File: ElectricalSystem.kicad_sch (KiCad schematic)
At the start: 2 parts, among them SW3 Supp_Enable

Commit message: update pedals
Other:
- sheet Pedal_Board ports: added Accel_Pot, Brake_Fluid, Brake_Pot; removed +3.3V_Accel, +3.3V_Brake, GND_Accel, GND_Brake, Sens_Accel, Sens_Brake
- note added: "- Controls Daughter Board - Steering board - Fans - Battery boards (internal HV?) - Telemetry sensors/leader - Array (MPPTs, Blackbody sensors) - VCU + MotorCAN? - Explain purpose of each CAN - Diagram CAN loop topology"
- note removed: "- Controls Daughter Board - Update pedals - Steering board - Fans - Battery boards (internal HV?) - Telemetry sensors/leader - Array (MPPTs, Blackbody sensors) - VCU + MotorCAN? - Explain purpose of each CAN - Diagram CAN loop topology"

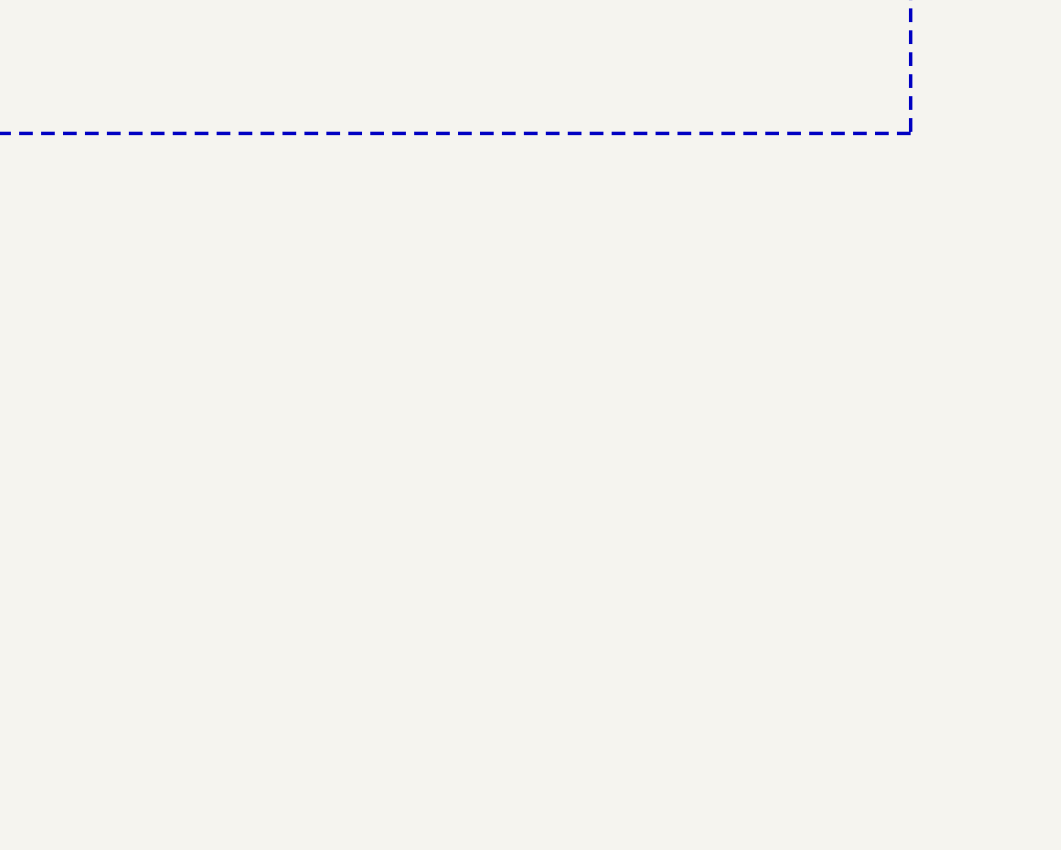
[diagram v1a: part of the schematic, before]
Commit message: start adding CAN topology notes
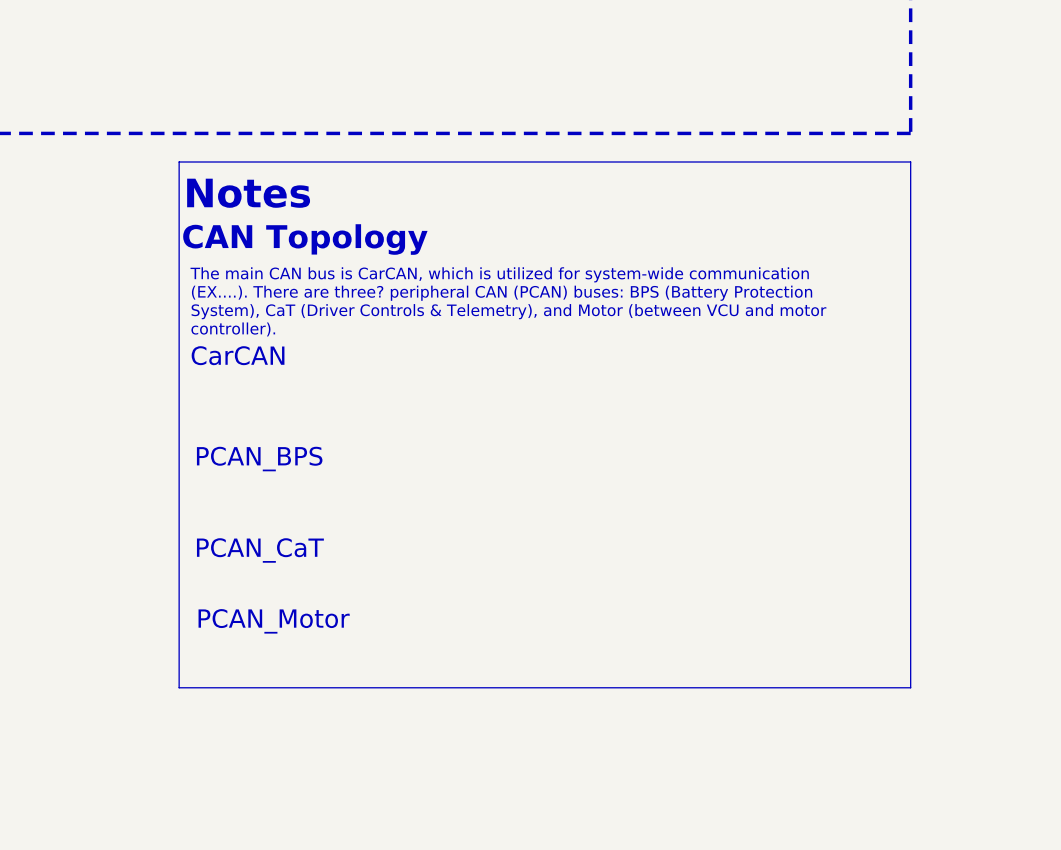
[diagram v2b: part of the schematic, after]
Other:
- note added: "CAN Topology"
- note added: "CarCAN"
- note added: "Notes"
- note added: "PCAN_BPS"
- note added: "PCAN_CaT"
- note added: "PCAN_Motor"
- note added: "The main CAN bus is CarCAN, which is utilized for system-wide communication (EX....). There are three? peripheral CAN (PCAN) buses: BPS (Battery Protection System), CaT (Driver Controls & Telemetry), and Motor (between VCU and motor controller)."
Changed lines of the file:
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@@
+	)
+	(rectangle
+		(start 462.28 137.16)
+		(end 543.56 195.58)
+		(stroke
+			(width 0)
+			(type default)
+		)
+		(fill
+			(type none)
+		)
 	)
 	(rectangle
@@
 		)
 	)
+	(text "The main CAN bus is CarCAN, which is utilized for system-wide communication\n(EX....). There are three? peripheral CAN (PCAN) buses: BPS (Battery Protection\nSystem), CaT (Driver Controls & Telemetry), and Motor (between VCU and motor\ncontroller)."
+		(exclude_from_sim no)
+		(at 463.55 152.908 0)
+		(effects
+			(font
+				(size 1.27 1.27)
+			)
+			(justify left)
+		)
+	)
 	(text "BPS"
 		(exclude_from_sim no)
@@
 		)
 	)
+	(text "CAN Topology"
+		(exclude_from_sim no)
+		(at 476.25 145.796 0)
+		(effects
+			(font
+				(size 2.54 2.54)
+				(bold yes)
+			)
+		)
+	)
 	(text "PDU and PowerBoard may be combined - TBD"
 		(exclude_from_sim no)
@@
 		)
 	)
+	(text "PCAN_Motor"
+		(exclude_from_sim no)
+		(at 472.694 188.214 0)
+		(effects
+			(font
+				(size 2.032 2.032)
+				(thickness 0.254)
+			)
+		)
+	)
 	(text "Cooling"
 		(exclude_from_sim no)
@@
 		)
 	)
+	(text "Notes"
+		(exclude_from_sim no)
+		(at 469.9 140.97 0)
+		(effects
+			(font
+				(size 3.175 3.175)
+				(bold yes)
+			)
+		)
+	)
 	(text "- Controls Daughter Board\n- Steering board\n- Fans\n- Battery boards (internal HV?)\n- Telemetry sensors/leader\n- Array (MPPTs, Blackbody sensors)\n- VCU + MotorCAN?\n- Explain purpose of each CAN\n- Diagram CAN loop topology"
 		(exclude_from_sim no)
@@
 		)
 	)
+	(text "PCAN_BPS"
+		(exclude_from_sim no)
+		(at 471.17 170.18 0)
+		(effects
+			(font
+				(size 2.032 2.032)
+				(thickness 0.254)
+			)
+		)
+	)
 	(text "add contactors, internal battery architecture, bus bar connections"
 		(exclude_from_sim no)
@@
 		)
 	)
+	(text "PCAN_CaT"
+		(exclude_from_sim no)
+		(at 471.17 180.34 0)
+		(effects
+			(font
+				(size 2.032 2.032)
+				(thickness 0.254)
+			)
+		)
+	)
 	(text "TODO:\n"
 		(exclude_from_sim no)
@@
 			)
 		)
+	)
+	(text "CarCAN"
+		(exclude_from_sim no)
+		(at 468.884 159.004 0)
+		(effects
+			(font
+				(size 2.032 2.032)
+				(thickness 0.254)
+			)
+		)

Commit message: add LV pwr dist
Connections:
- net SupplementalBattery/+12V_Supp: no longer SW3.1 (A)
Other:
- added sheet PeripheralSOM10 (PeripheralSOM.kicad_sch)
- added sheet PeripheralSOM11 (PeripheralSOM.kicad_sch)
- sheet Display_Screen ports: added LV_PWR; removed none
- sheet PowerDistributionBoard ports: added none; removed +5V_CarCAN, +CarCAN, -CarCAN, GND_CarCAN
- sheet SuppMonitoringBoard ports: added none; removed +5V_CarCAN, +CarCAN, -CarCAN, GND_CarCAN
- note added: "LV Power Distribution"
- note added: "Supp Enable switch on dashboard"
- moved on the sheet: SW3

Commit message: more stuff idk
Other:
- note added: "Array"
- note added: "HV Power Distribution"
- note added: "Main Battery Pack"
- note added: "Telemetry"
- note added: "add MPPTs, interface, blackbody A/C (temp/irradiance sensors)"
- note added: "add dynamics, environment, TPMS transceiver, broker?"
- note added: "replace with VCU and new architecture"
- note removed: "Battery"
- moved on the sheet: SW3

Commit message: heheheheh
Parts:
- added M1: Motor_BLDC, symbol Motor:Motor_DC
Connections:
- new net MotorController/PhaseA: M1.A (PhaseA)
- new net MotorController/PhaseB: M1.B (PhaseB)
- new net MotorController/PhaseC: M1.C (PhaseC)
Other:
- sheet MotorController ports: added DC+, DC-, PhaseA, PhaseB, PhaseC; removed none

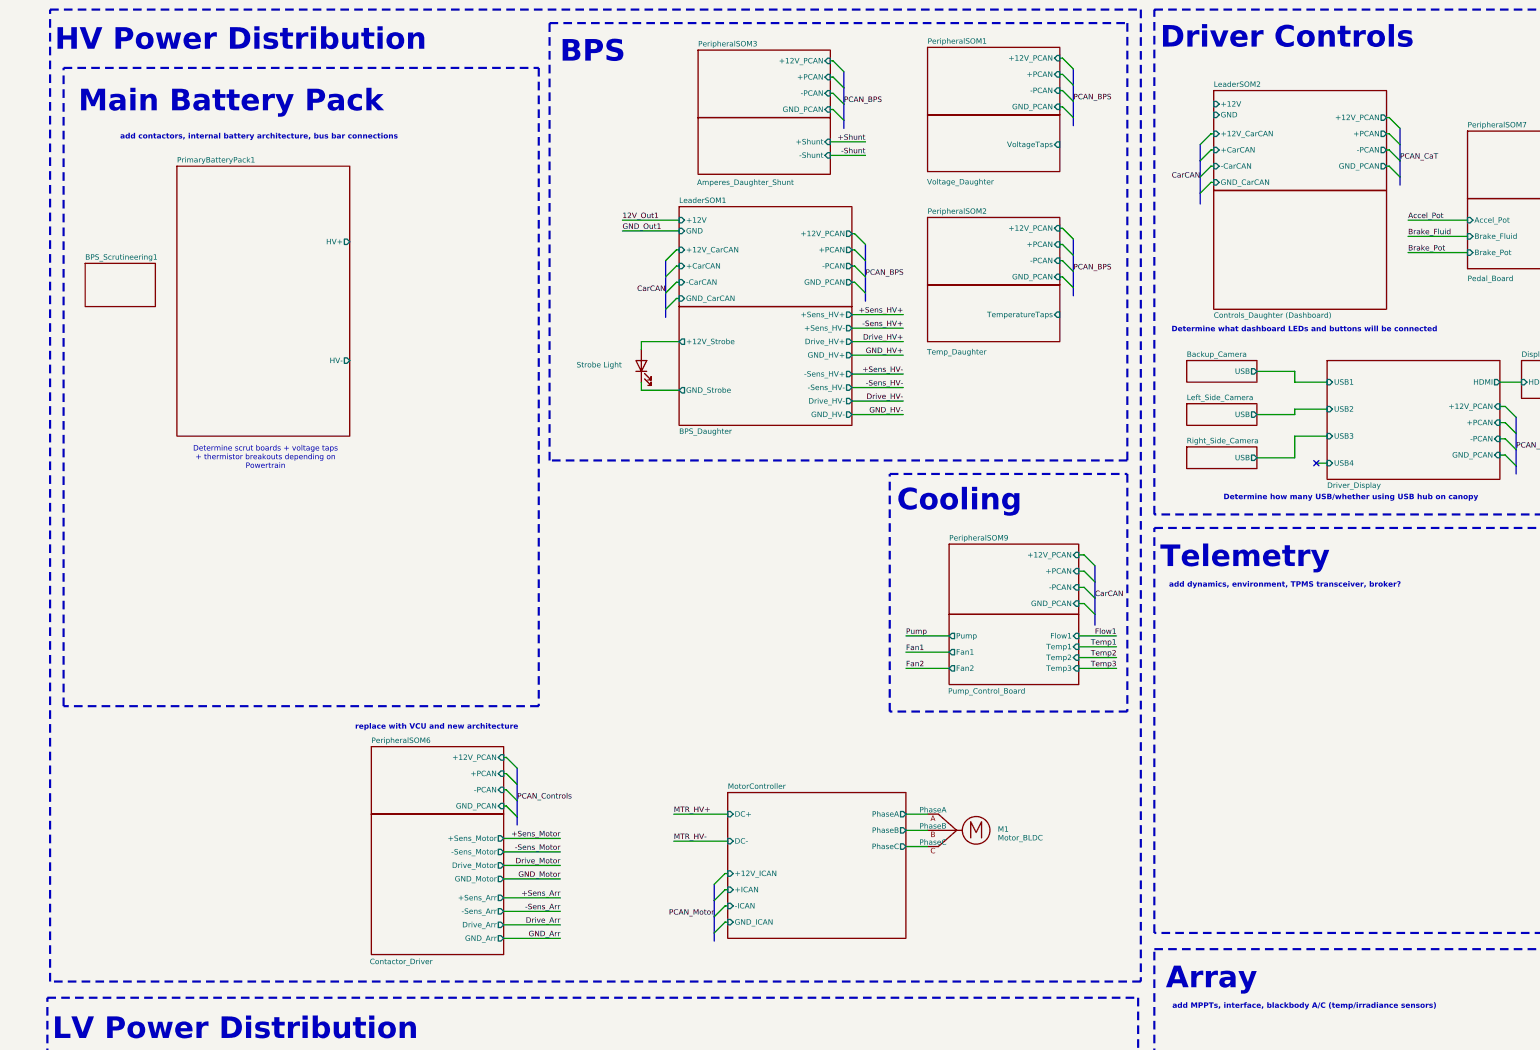
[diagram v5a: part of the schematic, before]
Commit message: moco intfc
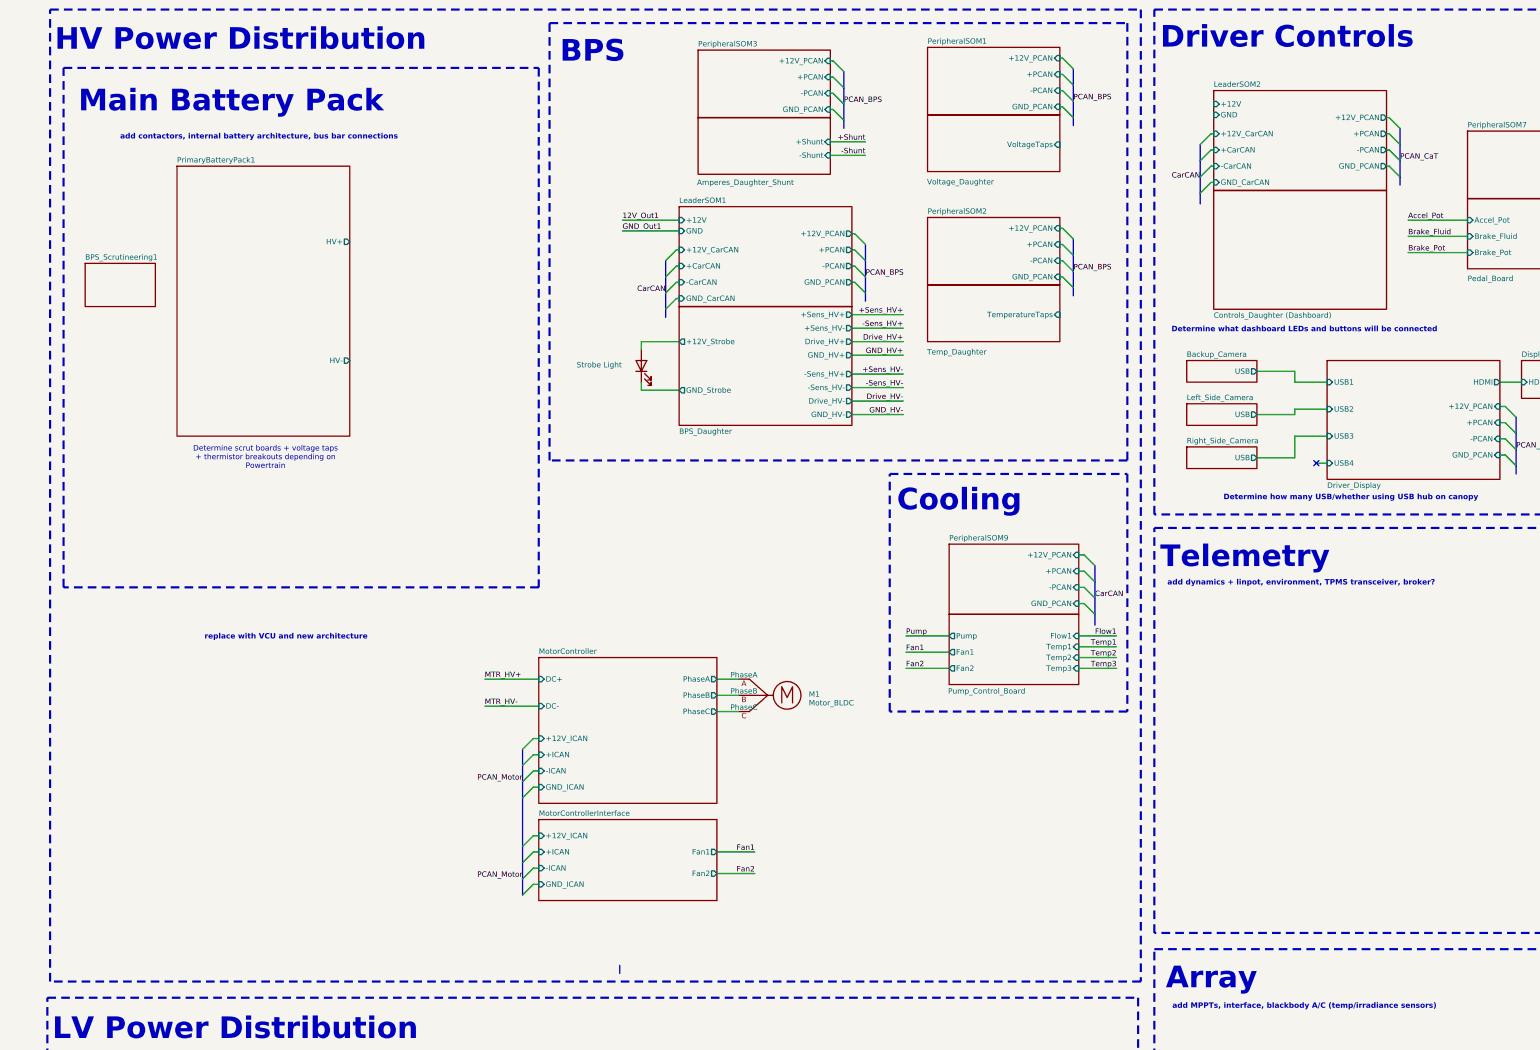
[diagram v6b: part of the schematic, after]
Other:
- removed sheet Contactor_Driver
- removed sheet PeripheralSOM6
- added sheet MotorControllerInterface (MotorControllerInterface.kicad_sch)
- note added: "add dynamics + linpot, environment, TPMS transceiver, broker?"
- note removed: "add dynamics, environment, TPMS transceiver, broker?"
- moved on the sheet: M1

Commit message: add mppts
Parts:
- added SC1, SC2, SC3: WHICH SUB ARRAY IS THIS, symbol Device:Solar_Cells
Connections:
- new net MPPT_A/PV+: SC1.1 (+)
- new net MPPT_A/PV-: SC1.2 (-)
- new net MPPT_B/PV+: SC2.1 (+)
- new net MPPT_B/PV-: SC2.2 (-)
- new net MPPT_C/PV+: SC3.1 (+)
- new net MPPT_C/PV-: SC3.2 (-)
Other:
- added sheet LeaderSOM3 (LeaderSOM.kicad_sch)
- added sheet MPPT_A (MPPT.kicad_sch)
- added sheet MPPT_B (MPPT.kicad_sch)
- added sheet MPPT_C (MPPT.kicad_sch)
- added sheet Steering_Board (Steering_Board.kicad_sch)
- added sheet VehicleControlUnit (VehicleControlUnit.kicad_sch)
- note added: "not sure if any of this needs isolation - check again!"

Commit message: wiring stuff
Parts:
- SC1: value WHICH SUB ARRAY IS THIS -> Rear_SubArray
- SC2: value WHICH SUB ARRAY IS THIS -> FrontRight_SubArray
- SC3: value WHICH SUB ARRAY IS THIS -> FrontLeft_SubArray
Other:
- sheet Display_Screen ports: added +12V, GND; removed LV_PWR
- note added: "High-Voltage High-Current (6 AWG)"
- note added: "High-Voltage Low-Current (14 AWG)"
- note added: "Low-Voltage High-Current (14 AWG)"
- note added: "Low-Voltage Low-Current (20 AWG)"
- note added: "PCAN_Controls"
- note added: "Wire Legend:"
- note added: "add blackbody A/C (temp/irradiance sensors)"
- note added: "add motor, motorpre, arraypre contactor drive/sense"
- note removed: "PCAN_CaT"
- note removed: "add MPPTs, interface, blackbody A/C (temp/irradiance sensors)"
- note removed: "replace with VCU and new architecture"
